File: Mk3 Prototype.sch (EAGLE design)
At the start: 163 parts, among them IC2 CC3100, IC3 S25FL216K0PMFI011, IC4 STM32F401V, IC6 AP3419, J1 ZX62-AB-5PA(11), J2 SWD_SHROUD, J7 SFV30R-2STE1HLF, Q1 BSS84W, Q11 BSS84W, Q12 2N7002KW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

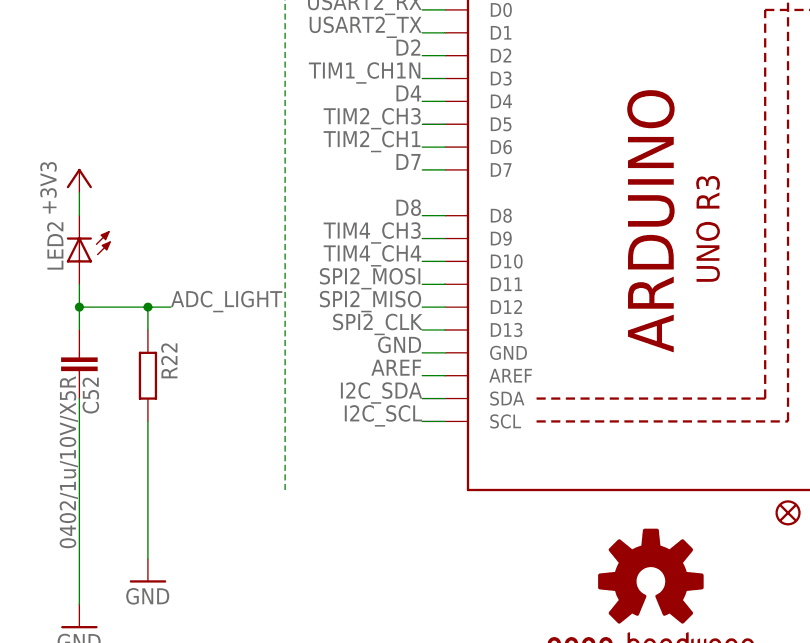
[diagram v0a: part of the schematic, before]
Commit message: made gpio headers stripbord happy
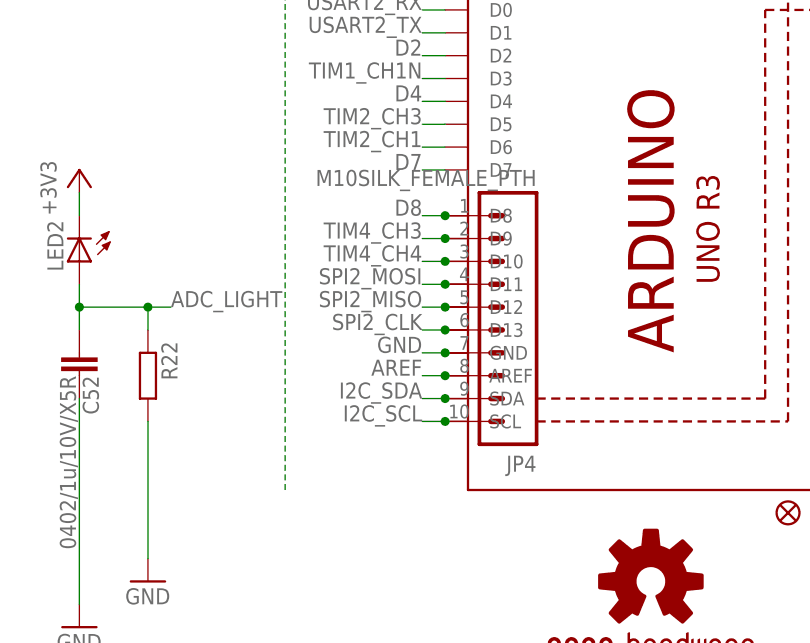
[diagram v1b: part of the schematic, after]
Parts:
- added JP4: M10SILK_FEMALE_PTH, SparkFun-Connectors:M10SILK_FEMALE_PTH
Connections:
- net AREF: now also JP4.8
- net D8: now also JP4.1
- net GND: now also JP4.7
- net I2C_SCL: now also JP4.10
- net I2C_SDA: now also JP4.9
- net SPI2_CLK: now also JP4.6
- net SPI2_MISO: now also JP4.5
- net SPI2_MOSI: now also JP4.4
- net TIM4_CH3: now also JP4.2
- net TIM4_CH4: now also JP4.3
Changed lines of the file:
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@@
 <part name="D1" library="TiLDA Mk3 Parts" deviceset="DIODE-" device="SOD123"/>
 <part name="SJ2" library="SparkFun-Passives" deviceset="JUMPER-PAD-2-NO" device="YES_SILK"/>
+<part name="JP4" library="SparkFun-Connectors" deviceset="M10" device="SILK_FEMALE_PTH"/>
 </parts>
 <sheets>
@@
 <attribute name="NAME" x="530.86" y="63.5" size="1.778" layer="95" rot="R180"/>
 </instance>
+<instance part="JP4" gate="G$1" x="317.5" y="38.1" rot="R180"/>
 </instances>
 <busses>
@@
 <label x="304.8" y="40.64" size="1.778" layer="95" rot="MR0"/>
 <pinref part="U4" gate="G$1" pin="GND"/>
+<pinref part="JP4" gate="G$1" pin="7"/>
+<junction x="307.34" y="40.64"/>
 </segment>
 <segment>
@@
 <label x="304.8" y="55.88" size="1.778" layer="95" rot="MR0"/>
 <pinref part="U4" gate="G$1" pin="D8"/>
+<pinref part="JP4" gate="G$1" pin="1"/>
+<junction x="307.34" y="55.88"/>
 </segment>
 <segment>
@@
 <label x="304.8" y="38.1" size="1.778" layer="95" rot="MR0"/>
 <pinref part="U4" gate="G$1" pin="AREF"/>
+<pinref part="JP4" gate="G$1" pin="8"/>
+<junction x="307.34" y="38.1"/>
 </segment>
 <segment>
@@
 <label x="304.8" y="45.72" size="1.778" layer="95" rot="MR0"/>
 <pinref part="U4" gate="G$1" pin="D12"/>
+<pinref part="JP4" gate="G$1" pin="5"/>
+<junction x="307.34" y="45.72"/>
 </segment>
 </net>
@@
 <label x="304.8" y="48.26" size="1.778" layer="95" rot="MR0"/>
 <pinref part="U4" gate="G$1" pin="D11"/>
+<pinref part="JP4" gate="G$1" pin="4"/>
+<junction x="307.34" y="48.26"/>
 </segment>
 </net>
@@
 <label x="304.8" y="43.18" size="1.778" layer="95" rot="MR0"/>
 <pinref part="U4" gate="G$1" pin="D13"/>
+<pinref part="JP4" gate="G$1" pin="6"/>
+<junction x="307.34" y="43.18"/>
 </segment>
 <segment>
@@
 <label x="304.8" y="35.56" size="1.778" layer="95" rot="MR0"/>
 <pinref part="U4" gate="G$1" pin="SDA"/>
+<pinref part="JP4" gate="G$1" pin="9"/>
+<junction x="307.34" y="35.56"/>
 </segment>
 </net>
@@
 <label x="304.8" y="50.8" size="1.778" layer="95" rot="MR0"/>
 <pinref part="U4" gate="G$1" pin="D10"/>
+<pinref part="JP4" gate="G$1" pin="3"/>
+<junction x="307.34" y="50.8"/>
 </segment>
 </net>
@@
 <label x="304.8" y="33.02" size="1.778" layer="95" rot="MR0"/>
 <pinref part="U4" gate="G$1" pin="SCL"/>
+<pinref part="JP4" gate="G$1" pin="10"/>
+<junction x="307.34" y="33.02"/>
 </segment>
 </net>
@@
 <label x="304.8" y="53.34" size="1.778" layer="95" rot="MR0"/>
 <pinref part="U4" gate="G$1" pin="D9"/>
-</segment>
-</net>
+<pinref part="JP4" gate="G$1" pin="2"/>
+<junction x="307.34" y="53.34"/>
+</segment>
+</net>

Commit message: musical spi ports complete
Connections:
- removed net JOY_CEN: IC4_PD.PD8, JP1.RIGHT
- removed net SPI4_MISO: IC2_HOST_SPI.MISO, IC4_PE.PE5
- removed net SPI4_NSS: IC2_HOST_SPI.!CS, IC4_PE.PE4
- removed net SPI4_SCK: IC2_HOST_SPI.CLK, IC4_PE.PE2
- removed net TIM5_CH1: IC4_PA.PA0, Q12.G
- new net JOY_RIGHT: IC4_PD.PD13, JP1.RIGHT
- new net SPI1_MISO: IC2_HOST_SPI.MISO, IC4_PA.PA6
- new net SPI1_NSS: IC2_HOST_SPI.!CS, IC4_PA.PA4
- new net SPI1_SCK: IC2_HOST_SPI.CLK, IC4_PA.PA5
- new net TIM9_CH1: IC4_PE.PE5, Q12.G
- net A0: now also IC4_PA.PA1; no longer IC4_PA.PA5
- net A1: now also IC4_PA.PA2; no longer IC4_PA.PA6
- net ADC_VBUS: now also IC4_PA.PA0; no longer IC4_PA.PA2
- net ADC_VIN: now also IC4_PC.PC3; no longer IC4_PA.PA4
- net MOM_UP: now also IC4_PE.PE4; no longer IC4_PA.PA1
- net SPI1_MOSI: now also IC2_HOST_SPI.MOSI; no longer D2.DIN
- net SPI4_MOSI: now also D2.DIN; no longer IC2_HOST_SPI.MOSI
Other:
- note added: "/ JOY_CEN"
- note added: "pull PB2 (BOOT1) low?"
- moved on the sheet: TP10, TP6, TP9

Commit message: rf bit changed
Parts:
- added R33: DNP (0ohm), TiLDA Mk3 Parts:R-EU_R0402-SMALLER
- added U$1: ANTENNA22500AT44M0400, SparkFun-RF:ANTENNA22500AT44M0400
- added X6: MC-921, con-coax:MC-921
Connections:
- new net ANT: C2.1, L1.2, U$1.SIGNAL
- new net N$48: R33.1, X6.1
- net GND: now also X6.GND@1; no longer C2.1, L1.2, Y1.1, Y1.GND
- net N$2: now also R33.2
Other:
- note removed: "add optional uFl connector?"
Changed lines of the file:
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@@
 <part name="SJ2" library="SparkFun-Passives" deviceset="JUMPER-PAD-2-NO" device="YES_SILK"/>
 <part name="JP4" library="SparkFun-Connectors" deviceset="M10" device="SILK_FEMALE_PTH"/>
+<part name="X6" library="con-coax" deviceset="MC-921" device=""/>
+<part name="R33" library="TiLDA Mk3 Parts" deviceset="R-EU_" device="R0402-SMALLER" value="DNP (0ohm)"/>
+<part name="GND95" library="TiLDA Mk3 Parts" deviceset="GND" device=""/>
+<part name="U$1" library="SparkFun-RF" deviceset="ANTENNA2" device="2500AT44M0400"/>
 </parts>
 <sheets>
@@
 <text x="655.32" y="175.26" size="1.778" layer="91">default: use stm32, DNP crystal + caps</text>
 <text x="266.7" y="111.76" size="1.778" layer="91">ESD!</text>
-<text x="739.14" y="251.46" size="1.778" layer="91">add optional uFl connector?</text>
 <text x="53.34" y="162.56" size="1.778" layer="91" rot="R90">SPI2</text>
 <wire x1="170.18" y1="50.8" x2="208.28" y2="50.8" width="0.1524" layer="97"/>
@@
 <text x="106.68" y="114.3" size="1.778" layer="91">/ JOY_CEN</text>
 <text x="797.56" y="185.42" size="2.54" layer="94">pull PB2 (BOOT1) low?</text>
+<text x="718.82" y="251.46" size="1.778" layer="91">spec</text>
+<text x="741.68" y="246.38" size="1.778" layer="91">spec</text>
 </plain>
 <instances>
@@
 </instance>
 <instance part="JP4" gate="G$1" x="317.5" y="38.1" rot="R180"/>
+<instance part="X6" gate="G$1" x="713.74" y="251.46" rot="MR0"/>
+<instance part="R33" gate="G$1" x="706.12" y="246.38" rot="R270"/>
+<instance part="GND95" gate="1" x="711.2" y="246.38"/>
+<instance part="U$1" gate="G$1" x="749.3" y="246.38"/>
 </instances>
 <busses>
@@
 </segment>
 <segment>
-<pinref part="Y1" gate="G$1" pin="GND"/>
-<wire x1="756.92" y1="243.84" x2="756.92" y2="241.3" width="0.1524" layer="91"/>
-<pinref part="GND11" gate="1" pin="GND"/>
-</segment>
-<segment>
 <pinref part="R1" gate="G$1" pin="2"/>
 <wire x1="762" y1="124.46" x2="762" y2="111.76" width="0.1524" layer="91"/>
@@
 </segment>
 <segment>
-<pinref part="L1" gate="G$1" pin="2"/>
-<wire x1="734.06" y1="241.3" x2="736.6" y2="241.3" width="0.1524" layer="91"/>
-<pinref part="C2" gate="G$1" pin="1"/>
-<wire x1="736.6" y1="241.3" x2="736.6" y2="238.76" width="0.1524" layer="91"/>
-<junction x="736.6" y="241.3"/>
-<pinref part="Y1" gate="G$1" pin="1"/>
-<wire x1="736.6" y1="241.3" x2="754.38" y2="241.3" width="0.1524" layer="91"/>
-<wire x1="754.38" y1="238.76" x2="754.38" y2="241.3" width="0.1524" layer="91"/>
-<pinref part="GND43" gate="1" pin="GND"/>
-<junction x="754.38" y="241.3"/>
-<wire x1="754.38" y1="241.3" x2="754.38" y2="243.84" width="0.1524" layer="91"/>
-</segment>
-<segment>
 <pinref part="R10" gate="G$1" pin="2"/>
 <wire x1="764.54" y1="53.34" x2="764.54" y2="38.1" width="0.1524" layer="91"/>
@@
 <pinref part="GND94" gate="1" pin="GND"/>
 </segment>
+<segment>
+<pinref part="X6" gate="G$1" pin="GND@1"/>
+<pinref part="GND95" gate="1" pin="GND"/>
+</segment>
 </net>
 <net name="F1" class="0">
@@
 </segment>
 </net>
-<net name="N$3" class="0">
+<net name="N$3" class="1">
 <segment>
 <pinref part="FL1" gate="G$1" pin="IN"/>
@@
 <segment>
 <pinref part="FL1" gate="G$1" pin="OUT"/>
-<wire x1="693.42" y1="241.3" x2="716.28" y2="241.3" width="0.1524" layer="91"/>
+<wire x1="693.42" y1="241.3" x2="706.12" y2="241.3" width="0.1524" layer="91"/>
 <pinref part="L1" gate="G$1" pin="1"/>
 <pinref part="C1" gate="G$1" pin="1"/>
+<wire x1="706.12" y1="241.3" x2="716.28" y2="241.3" width="0.1524" layer="91"/>
 <wire x1="716.28" y1="241.3" x2="718.82" y2="241.3" width="0.1524" layer="91"/>
 <wire x1="716.28" y1="241.3" x2="716.28" y2="238.76" width="0.1524" layer="91"/>
 <junction x="716.28" y="241.3"/>
+<pinref part="R33" gate="G$1" pin="2"/>
+<junction x="706.12" y="241.3"/>
 </segment>
 </net>
@@
 </segment>
 </net>
+<net name="N$48" class="1">
+<segment>
+<pinref part="R33" gate="G$1" pin="1"/>
+<pinref part="X6" gate="G$1" pin="1"/>
+<wire x1="706.12" y1="251.46" x2="711.2" y2="251.46" width="0.1524" layer="91"/>
+</segment>
+</net>
+<net name="ANT" class="1">
+<segment>
+<pinref part="L1" gate="G$1" pin="2"/>
+<wire x1="734.06" y1="241.3" x2="736.6" y2="241.3" width="0.1524" layer="91"/>
+<pinref part="C2" gate="G$1" pin="1"/>
+<wire x1="736.6" y1="241.3" x2="736.6" y2="238.76" width="0.1524" layer="91"/>
+<junction x="736.6" y="241.3"/>
+<wire x1="736.6" y1="241.3" x2="749.3" y2="241.3" width="0.1524" layer="91"/>
+<wire x1="749.3" y1="241.3" x2="754.38" y2="241.3" width="0.1524" layer="91"/>
+<wire x1="754.38" y1="238.76" x2="754.38" y2="241.3" width="0.1524" layer="91"/>
+<pinref part="GND43" gate="1" pin="GND"/>
+<pinref part="U$1" gate="G$1" pin="SIGNAL"/>
+<junction x="749.3" y="241.3"/>
+</segment>
+</net>

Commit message: a little more decoupling
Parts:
- added C62, C63, C64: 0402/4u7/10V/X5R, TiLDA Mk3 Parts:C-EUC0402-SMALLER
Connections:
- new net N$49: C64.2, D2.VDD
- net +3V3: now also C62.2, C63.2
- net GND: now also C62.1, C63.1, C64.1
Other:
- note removed: "decouple"
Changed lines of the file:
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@@
 <part name="GND95" library="TiLDA Mk3 Parts" deviceset="GND" device=""/>
 <part name="U$1" library="SparkFun-RF" deviceset="ANTENNA2" device="2500AT44M0400"/>
+<part name="C62" library="TiLDA Mk3 Parts" deviceset="C-EU" device="C0402-SMALLER" value="0402/4u7/10V/X5R"/>
+<part name="C63" library="TiLDA Mk3 Parts" deviceset="C-EU" device="C0402-SMALLER" value="0402/4u7/10V/X5R"/>
+<part name="GND96" library="TiLDA Mk3 Parts" deviceset="GND" device=""/>
+<part name="C64" library="TiLDA Mk3 Parts" deviceset="C-EU" device="C0402-SMALLER" value="0402/4u7/10V/X5R"/>
+<part name="GND97" library="TiLDA Mk3 Parts" deviceset="GND" device=""/>
 </parts>
 <sheets>
@@
 <text x="797.56" y="223.52" size="2.54" layer="94">SDIO_SW can be easily changed away from pin PC13</text>
 <text x="585.724" y="93.218" size="1.778" layer="91" rot="R90">connect these three </text>
-<text x="632.46" y="137.16" size="1.778" layer="91">decouple</text>
-<text x="543.56" y="116.84" size="1.778" layer="91">decouple</text>
 <text x="462.28" y="119.38" size="1.778" layer="91">also connect
 to a gpio</text>
@@
 <instance part="GND95" gate="1" x="711.2" y="246.38"/>
 <instance part="U$1" gate="G$1" x="749.3" y="246.38"/>
+<instance part="C62" gate="G$1" x="248.92" y="200.66" rot="R180"/>
+<instance part="C63" gate="G$1" x="645.16" y="132.08" rot="R180"/>
+<instance part="GND96" gate="1" x="645.16" y="127"/>
+<instance part="C64" gate="G$1" x="538.48" y="121.92" rot="R270"/>
+<instance part="GND97" gate="1" x="543.56" y="121.92" rot="R90"/>
 </instances>
 <busses>
@@
 <pinref part="GND79" gate="1" pin="GND"/>
 <pinref part="C9" gate="G$1" pin="1"/>
-<wire x1="243.84" y1="198.12" x2="243.84" y2="180.34" width="0.1524" layer="91"/>
+<wire x1="243.84" y1="198.12" x2="243.84" y2="195.58" width="0.1524" layer="91"/>
+<pinref part="C62" gate="G$1" pin="1"/>
+<wire x1="243.84" y1="195.58" x2="243.84" y2="180.34" width="0.1524" layer="91"/>
+<wire x1="248.92" y1="198.12" x2="248.92" y2="195.58" width="0.1524" layer="91"/>
+<wire x1="248.92" y1="195.58" x2="243.84" y2="195.58" width="0.1524" layer="91"/>
+<junction x="243.84" y="195.58"/>
 </segment>
 <segment>
@@
 <pinref part="GND95" gate="1" pin="GND"/>
 </segment>
+<segment>
+<pinref part="C63" gate="G$1" pin="1"/>
+<pinref part="GND96" gate="1" pin="GND"/>
+</segment>
+<segment>
+<pinref part="C64" gate="G$1" pin="1"/>
+<pinref part="GND97" gate="1" pin="GND"/>
+</segment>
 </net>
 <net name="F1" class="0">
@@
 <junction x="243.84" y="210.82"/>
 <junction x="243.84" y="208.28"/>
+<pinref part="C62" gate="G$1" pin="2"/>
+<wire x1="248.92" y1="205.74" x2="248.92" y2="208.28" width="0.1524" layer="91"/>
+<wire x1="248.92" y1="208.28" x2="243.84" y2="208.28" width="0.1524" layer="91"/>
 </segment>
 <segment>
@@
 <pinref part="X5" gate="G$1" pin="VCC"/>
 <pinref part="+3V11" gate="G$1" pin="+3V3"/>
+<pinref part="C63" gate="G$1" pin="2"/>
+<wire x1="629.92" y1="137.16" x2="645.16" y2="137.16" width="0.1524" layer="91"/>
+<junction x="629.92" y="137.16"/>
 </segment>
 <segment>
@@
 </segment>
 </net>
+<net name="N$49" class="0">
+<segment>
+<pinref part="D2" gate="G$1" pin="VDD"/>
+<wire x1="535.94" y1="111.76" x2="530.86" y2="111.76" width="0.1524" layer="91"/>
+<wire x1="530.86" y1="111.76" x2="530.86" y2="121.92" width="0.1524" layer="91"/>
+<junction x="530.86" y="121.92"/>
+<wire x1="530.86" y1="121.92" x2="530.86" y2="127" width="0.1524" layer="91"/>
+<pinref part="C64" gate="G$1" pin="2"/>
+<wire x1="533.4" y1="121.92" x2="530.86" y2="121.92" width="0.1524" layer="91"/>
+</segment>
+</net>

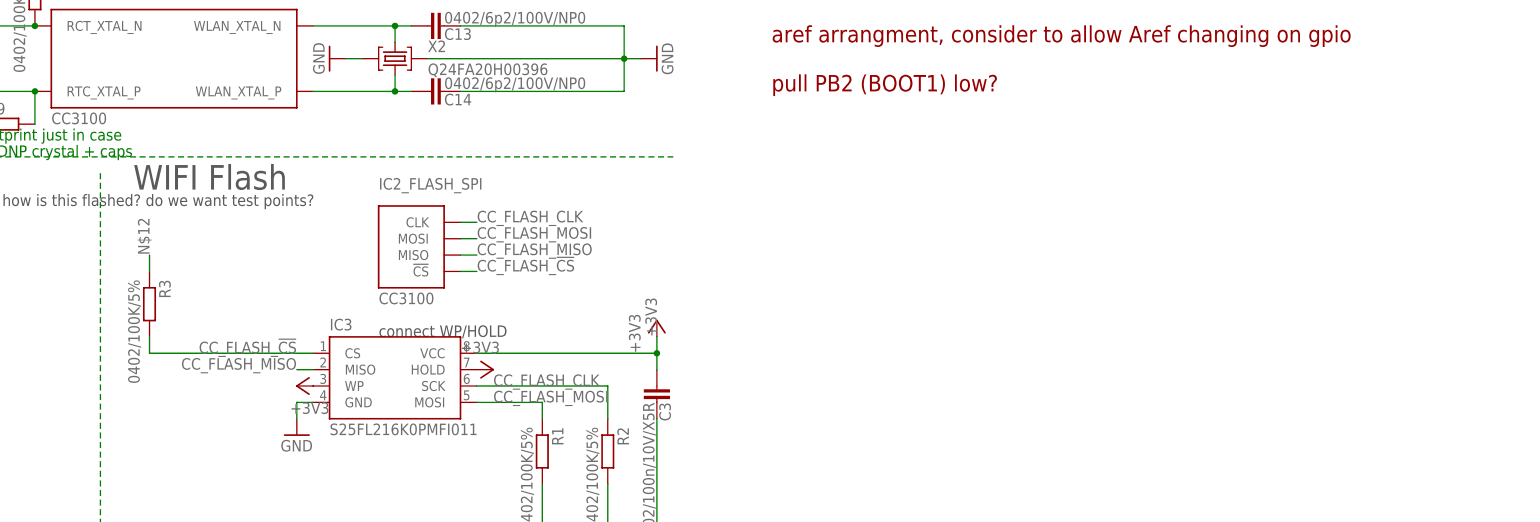
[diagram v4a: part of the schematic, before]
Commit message: improved placement of flash IC
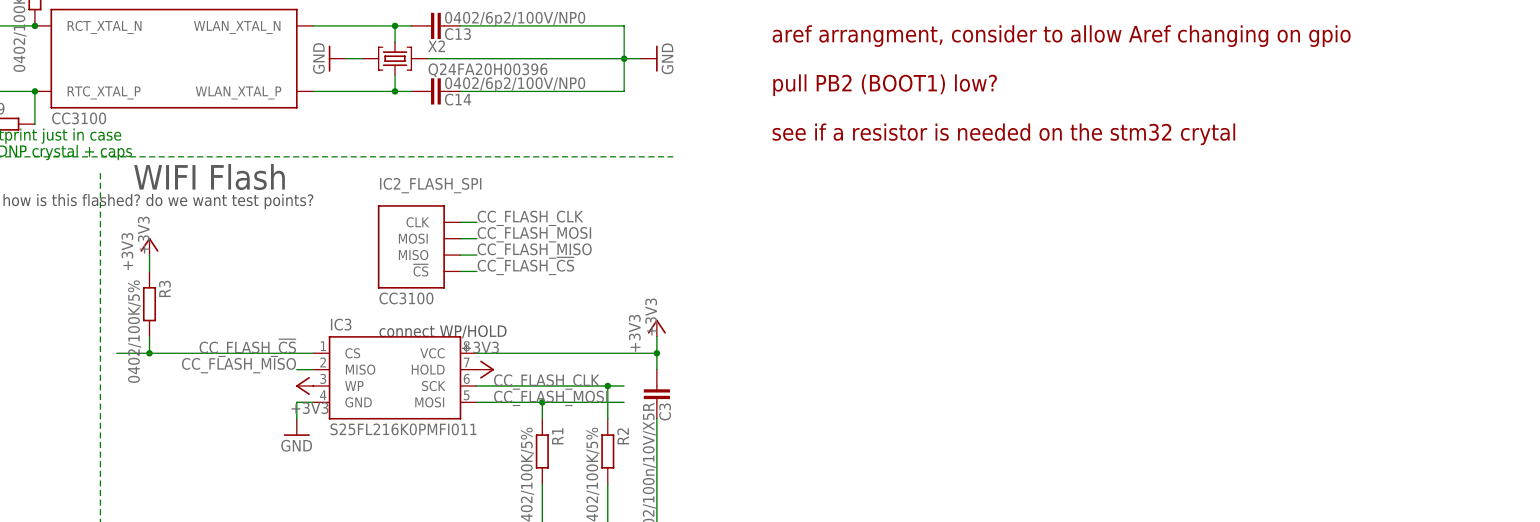
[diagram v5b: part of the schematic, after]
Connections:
- removed net N$12: R3.1
- net +3V3: now also R3.1
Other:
- note added: "see if a resistor is needed on the stm32 crytal"
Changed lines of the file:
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@@
 <part name="C64" library="TiLDA Mk3 Parts" deviceset="C-EU" device="C0402-SMALLER" value="0402/4u7/10V/X5R"/>
 <part name="GND97" library="TiLDA Mk3 Parts" deviceset="GND" device=""/>
+<part name="+3V21" library="supply1" deviceset="+3V3" device=""/>
 </parts>
 <sheets>
@@
 <text x="718.82" y="251.46" size="1.778" layer="91">spec</text>
 <text x="741.68" y="246.38" size="1.778" layer="91">spec</text>
+<text x="797.56" y="177.8" size="2.54" layer="94">see if a resistor is needed on the stm32 crytal</text>
 </plain>
 <instances>
@@
 <instance part="C64" gate="G$1" x="538.48" y="121.92" rot="R270"/>
 <instance part="GND97" gate="1" x="543.56" y="121.92" rot="R90"/>
+<instance part="+3V21" gate="G$1" x="701.04" y="162.56"/>
 </instances>
 <busses>
@@
 <wire x1="726.44" y1="144.78" x2="701.04" y2="144.78" width="0.1524" layer="91"/>
 <wire x1="701.04" y1="144.78" x2="701.04" y2="147.32" width="0.1524" layer="91"/>
+<wire x1="701.04" y1="144.78" x2="695.96" y2="144.78" width="0.1524" layer="91"/>
+<junction x="701.04" y="144.78"/>
 </segment>
 </net>
@@
 <wire x1="762" y1="137.16" x2="762" y2="134.62" width="0.1524" layer="91"/>
 <wire x1="762" y1="137.16" x2="751.84" y2="137.16" width="0.1524" layer="91"/>
+<wire x1="762" y1="137.16" x2="774.7" y2="137.16" width="0.1524" layer="91"/>
+<junction x="762" y="137.16"/>
 </segment>
 <segment>
@@
 <wire x1="751.84" y1="139.7" x2="772.16" y2="139.7" width="0.1524" layer="91"/>
 <wire x1="772.16" y1="139.7" x2="772.16" y2="134.62" width="0.1524" layer="91"/>
+<wire x1="772.16" y1="139.7" x2="774.7" y2="139.7" width="0.1524" layer="91"/>
+<junction x="772.16" y="139.7"/>
 </segment>
 <segment>
@@
 <wire x1="751.84" y1="165.1" x2="749.3" y2="165.1" width="0.1524" layer="91"/>
 <label x="751.84" y="165.1" size="1.778" layer="95"/>
-</segment>
-</net>
-<net name="N$12" class="0">
-<segment>
-<pinref part="R3" gate="G$1" pin="1"/>
-<wire x1="701.04" y1="157.48" x2="701.04" y2="160.02" width="0.1524" layer="91"/>
-<label x="701.04" y="160.02" size="1.778" layer="95" rot="R90"/>
 </segment>
 </net>
@@
 <junction x="627.38" y="45.72"/>
 </segment>
-</net>
+<segment>
+<pinref part="R3" gate="G$1" pin="1"/>
+<wire x1="701.04" y1="157.48" x2="701.04" y2="160.02" width="0.1524" layer="91"/>
+<label x="701.04" y="160.02" size="1.778" layer="95" rot="R90"/>
+<pinref part="+3V21" gate="G$1" pin="+3V3"/>
+</segment>
+</net>
